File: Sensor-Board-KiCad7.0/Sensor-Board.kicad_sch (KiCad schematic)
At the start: 73 parts, among them J1 B4B-XH-A, U1 OPA396DCKT, U10 BME680, U13 TCA9548AMRGER, U14 OPA396DCKT, U19 MMBFJ177LT1, U2 OPA396DCKT, U20 MMBFJ177LT1, U21 OPA396DCKT, U22 OPA396DCKT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

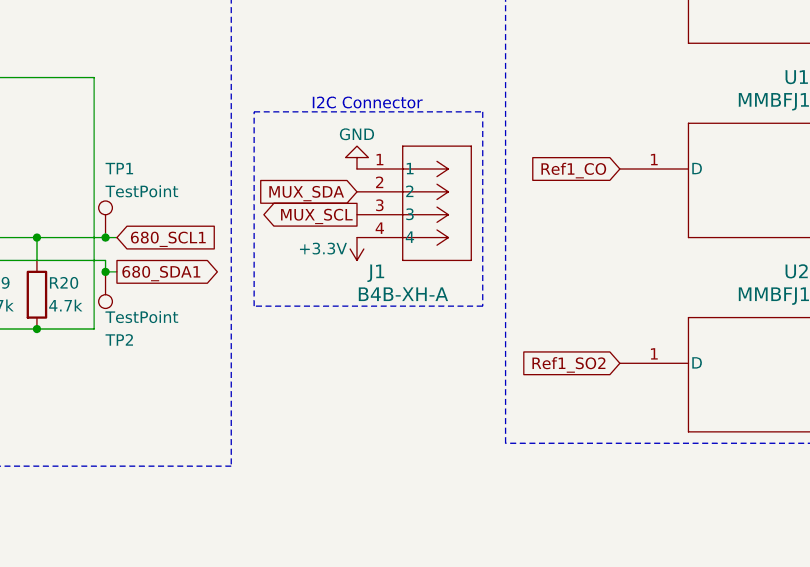
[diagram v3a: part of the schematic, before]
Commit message: Traces all connected v1.0
Restarted the process of routing traces (didn't account for width of 3.3V traces in first attempt). Everything is now connected for first time.
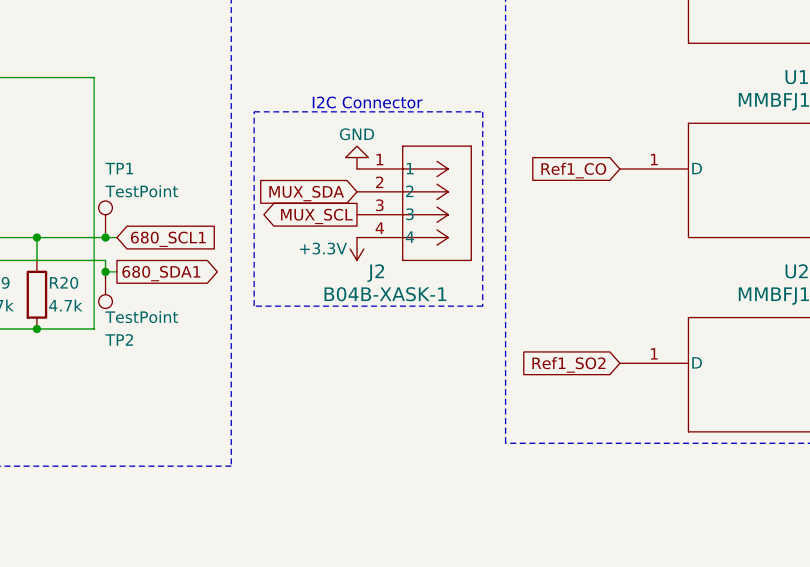
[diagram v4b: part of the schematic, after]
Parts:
- removed J1: B4B-XH-A, I2C Connector:CONN_B4B-XH-A_JST, symbol I2C Connector:B4B-XH-A
- added J2: B04B-XASK-1, B04B_XASK1:CONN_B04B-XASK-1_JST, symbol B04B_XASK_1:B04B-XASK-1
- U23: Digikey (none) -> ED90102-ND
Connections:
- net +3.3V: now also J2.4
- net GND: now also J2.1
- net MUX_SCL: now also J2.3
- net MUX_SDA: now also J2.2
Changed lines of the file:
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@@
       (effects (font (size 1.27 1.27)) hide)
     )
-    (property "Datasheet" "" (at 198.12 160.02 0)
+    (property "Datasheet" "ED90102-ND" (at 198.12 160.02 0)
       (effects (font (size 1.27 1.27)) hide)
     )
@@
       (effects (font (size 1.27 1.27)) hide)
     )
-    (property "Datasheet" "" (at 198.12 137.16 0)
+    (property "Datasheet" "ED90102-ND" (at 198.12 137.16 0)
       (effects (font (size 1.27 1.27)) hide)
     )
@@
       (effects (font (size 1.27 1.27)) hide)
     )
+    (property "Digikey" "ED90102-ND" (at 198.12 114.3 0)
+      (effects (font (size 1.27 1.27)) hide)
+    )
     (pin "3")
     (pin "1")
@@
     )
   )
+  (symbol (lib_id "B04B_XASK_1:B04B-XASK-1") (at 91.44 162.56 0) (unit 1)
+    (in_bom yes) (on_board yes) (dnp no)
+    (property "Reference" "J2" (at 92.71 173.99 0)
+      (effects (font (size 1.524 1.524)) (justify left))
+    )
+    (property "Value" "B04B-XASK-1" (at 87.63 176.53 0)
+      (effects (font (size 1.524 1.524)) (justify left))
+    )
+    (property "Footprint" "B04B_XASK1:CONN_B04B-XASK-1_JST" (at 88.9 156.21 0)
+      (effects (font (size 1.27 1.27) italic) hide)
+    )
+    (property "Datasheet" "B04B-XASK-1" (at 88.9 157.48 0)
+      (effects (font (size 1.27 1.27) italic) hide)
+    )
+    (property "LCSC" "C264994" (at 91.44 162.56 0)
+      (effects (font (size 1.27 1.27)) hide)
+    )
+    (pin "3")
+    (pin "1")
+    (pin "4")
+    (pin "2")
+    (instances
+      (project "Sensor-Board"
+        (path "/3a986dcd-349f-492d-950a-09832b2e5abd"
+          (reference "J2") (unit 1)
+        )
+      )
+    )
+  )
   (symbol (lib_id "Device:R") (at 109.22 77.47 270) (unit 1)
     (in_bom yes) (on_board yes) (dnp no)
@@
         )
       )
-    )
-  )
-  (symbol (lib_id "I2C Connector:B4B-XH-A") (at 91.44 162.56 0) (unit 1)
-    (in_bom yes) (on_board yes) (dnp no)
-    (property "Reference" "J1" (at 92.71 173.99 0)
-      (effects (font (size 1.524 1.524)) (justify left))
-    )
-    (property "Value" "B4B-XH-A" (at 91.44 176.53 0)
-      (effects (font (size 1.524 1.524)) (justify left))
-    )
-    (property "Footprint" "I2C Connector:CONN_B4B-XH-A_JST" (at 87.63 157.48 0)
-      (effects (font (size 1.27 1.27) italic) hide)
-    )
-    (property "Datasheet" "B4B-XH-A" (at 87.63 160.02 0)
-      (effects (font (size 1.27 1.27) italic) hide)
-    )
-    (pin "2")
-    (pin "4")
-    (pin "1")
-    (pin "3")
-    (instances
-      (project "Sensor-Board"
-        (path "/3a986dcd-349f-492d-950a-09832b2e5abd"
-          (reference "J1") (unit 1)
-        )
-      )

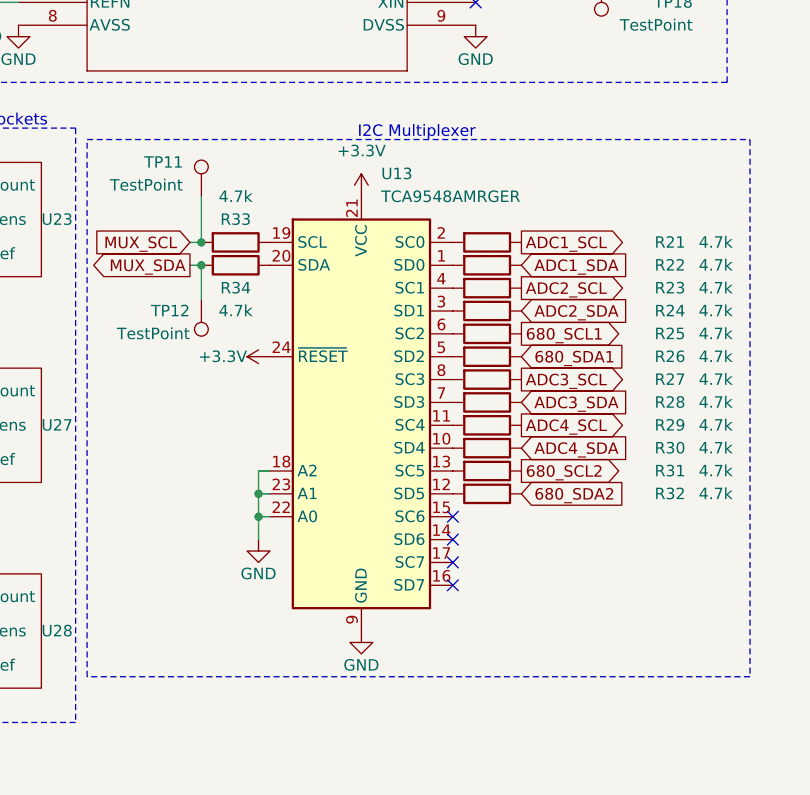
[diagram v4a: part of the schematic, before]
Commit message: Replaced TCA9548 footprint
Replaced TCA9548 footprint and added LCSC + Digikey numbers for all remaining symbols in schematic
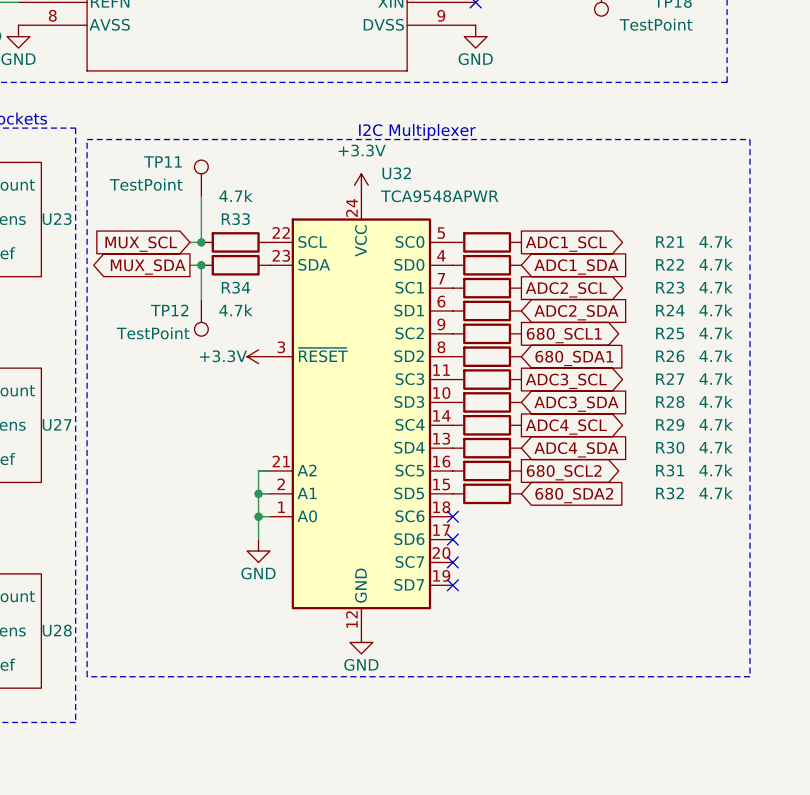
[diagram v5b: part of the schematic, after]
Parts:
- removed U13: TCA9548AMRGER, Package_DFN_QFN:Texas_RGE0024C_VQFN-24-1EP_4x4mm_P0.5mm_EP2.1x2.1mm, symbol Interface_Expansion:TCA9548AMRGER
- added U32: TCA9548APWR, Package_SO:TSSOP-24_4.4x7.8mm_P0.65mm, symbol Interface_Expansion:TCA9548APWR
- U1, U14, U21, U22: Digikey (none) -> 296-OPA396DCKRCT-ND
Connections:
- net +3.3V: now also U32.24 (VCC), U32.3 (~{RESET})
- net GND: now also U32.1 (A0), U32.12 (GND), U32.2 (A1), U32.21 (A2)
- net at R22.2: now also U32.4 (SD0)
- net at R30.2: now also U32.13 (SD4)
- net at R29.2: now also U32.14 (SC4)
- net at R32.2: now also U32.15 (SD5)
- net at R31.2: now also U32.16 (SC5)
- net at R33.1: now also U32.22 (SCL)
- net at R21.2: now also U32.5 (SC0)
- net at R34.1: now also U32.23 (SDA)
- net at R24.2: now also U32.6 (SD1)
- net at R23.2: now also U32.7 (SC1)
- net at R26.2: now also U32.8 (SD2)
- net at R25.2: now also U32.9 (SC2)
- net at R28.2: now also U32.10 (SD3)
- net at R27.2: now also U32.11 (SC3)
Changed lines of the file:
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@@
       (effects (font (size 1.27 1.27) italic) hide)
+    )
+    (property "Digikey" "296-OPA396DCKRCT-ND" (at 40.64 88.9 0)
+      (effects (font (size 1.27 1.27)) hide)
     )
     (pin "1")
@@
     )
   )
-  (symbol (lib_id "Interface_Expansion:TCA9548AMRGER") (at 240.03 128.27 0) (unit 1)
-    (in_bom yes) (on_board yes) (dnp no) (fields_autoplaced)
-    (property "Reference" "U13" (at 242.2241 102.87 0)
-      (effects (font (size 1.27 1.27)) (justify left))
-    )
-    (property "Value" "TCA9548AMRGER" (at 242.2241 105.41 0)
-      (effects (font (size 1.27 1.27)) (justify left))
-    )
-    (property "Footprint" "Package_DFN_QFN:Texas_RGE0024C_VQFN-24-1EP_4x4mm_P0.5mm_EP2.1x2.1mm" (at 240.03 153.67 0)
-      (effects (font (size 1.27 1.27)) hide)
-    )
-    (property "Datasheet" "http://www.ti.com/lit/ds/symlink/tca9548a.pdf" (at 241.3 121.92 0)
-      (effects (font (size 1.27 1.27)) hide)
-    )
-    (pin "10")
-    (pin "4")
-    (pin "14")
-    (pin "1")
-    (pin "2")
-    (pin "9")
-    (pin "5")
-    (pin "18")
-    (pin "12")
-    (pin "23")
-    (pin "8")
-    (pin "21")
-    (pin "25")
-    (pin "13")
-    (pin "11")
-    (pin "15")
-    (pin "16")
-    (pin "19")
-    (pin "20")
-    (pin "3")
-    (pin "17")
-    (pin "24")
-    (pin "6")
-    (pin "7")
-    (pin "22")
-    (instances
-      (project "Sensor-Board"
-        (path "/3a986dcd-349f-492d-950a-09832b2e5abd"
-          (reference "U13") (unit 1)
-        )
-      )
-    )
-  )
   (symbol (lib_id "Device:R") (at 254 135.89 270) (unit 1)
     (in_bom yes) (on_board yes) (dnp no)
@@
     (property "Datasheet" "OPA396DCKT" (at 40.64 130.81 0)
       (effects (font (size 1.27 1.27) italic) hide)
+    )
+    (property "Digikey" "296-OPA396DCKRCT-ND" (at 40.64 130.81 0)
+      (effects (font (size 1.27 1.27)) hide)
     )
     (pin "1")
@@
     (property "Datasheet" "OPA396DCKT" (at 113.03 77.47 0)
       (effects (font (size 1.27 1.27) italic) hide)
+    )
+    (property "Digikey" "" (at 113.03 77.47 0)
+      (effects (font (size 1.27 1.27)) hide)
     )
     (pin "1")
@@
       (effects (font (size 1.27 1.27) italic) hide)
     )
+    (property "Digikey" "296-OPA396DCKRCT-ND" (at 111.76 41.91 0)
+      (effects (font (size 1.27 1.27)) hide)
+    )
     (pin "1")
     (pin "3")
@@
       (effects (font (size 1.27 1.27) italic) hide)
     )
+    (property "Digikey" "296-OPA396DCKRCT-ND" (at 40.64 46.99 0)
+      (effects (font (size 1.27 1.27)) hide)
+    )
     (pin "1")
     (pin "3")
@@
       (effects (font (size 1.27 1.27) italic) hide)
     )
+    (property "Digikey" "" (at 113.03 113.03 0)
+      (effects (font (size 1.27 1.27)) hide)
+    )
     (pin "1")
     (pin "3")
@@
         )
       )
+    )
+  )
+  (symbol (lib_id "Interface_Expansion:TCA9548APWR") (at 240.03 128.27 0) (unit 1)
+    (in_bom yes) (on_board yes) (dnp no) (fields_autoplaced)
+    (property "Reference" "U32" (at 242.2241 102.87 0)
+      (effects (font (size 1.27 1.27)) (justify left))
+    )
+    (property "Value" "TCA9548APWR" (at 242.2241 105.41 0)
+      (effects (font (size 1.27 1.27)) (justify left))
+    )
+    (property "Footprint" "Package_SO:TSSOP-24_4.4x7.8mm_P0.65mm" (at 240.03 153.67 0)
+      (effects (font (size 1.27 1.27)) hide)
+    )
+    (property "Datasheet" "http://www.ti.com/lit/ds/symlink/tca9548a.pdf" (at 241.3 121.92 0)
+      (effects (font (size 1.27 1.27)) hide)
+    )
+    (property "LCSC" "C130026" (at 240.03 128.27 0)
+      (effects (font (size 1.27 1.27)) hide)
+    )
+    (pin "20")
+    (pin "23")
+    (pin "19")
+    (pin "4")
+    (pin "7")
+    (pin "12")
+    (pin "21")
+    (pin "8")
+    (pin "14")
+    (pin "6")
+    (pin "17")
+    (pin "11")
+    (pin "15")
+    (pin "18")
+    (pin "22")
+    (pin "1")
+    (pin "10")
+    (pin "2")
+    (pin "5")
+    (pin "13")
+    (pin "16")
+    (pin "24")
+    (pin "3")
+    (pin "9")
+    (instances
+      (project "Sensor-Board"
+        (path "/3a986dcd-349f-492d-950a-09832b2e5abd"
+          (reference "U32") (unit 1)
+        )
+      )

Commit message: Updated gas collection cell drawing
Updated GCC drawing to bring it to actual size
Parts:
- J2: Digikey (none) -> 455-2150-ND
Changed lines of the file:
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@@
+      (effects (font (size 1.27 1.27)) hide)
+    )
+    (property "Digikey" "455-2150-ND" (at 91.44 162.56 0)
       (effects (font (size 1.27 1.27)) hide)
     )

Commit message: Updated page settings
Added details such as contributors, Rev. number, board name, etc...
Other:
- company: (none) -> Queen's Rocket Engineering Team
- title: (none) -> Payload Sensor Board
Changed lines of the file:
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@@
 (kicad_sch (version 20230121) (generator eeschema)
   (paper "A4")
+  (title_block
+    (title "Payload Sensor Board")
+    (date "2024-03-23")
+    (rev "1.0")
+    (company "Queen's Rocket Engineering Team")
+    (comment 1 "Contributors: Kennan Bays, Joachim Blohm, Rowan Burke, Mohamad Gapre, Dominic Kilpatrick, Ben Taylor")
+  )
   (junction (at 153.67 67.31) (diameter 0) (color 0 0 0 0)
   )

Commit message: Updated part numbers
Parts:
- C4: LCSC (none) -> C140966
- J2: Digikey 455-2150-ND -> (none)
- U19, U20, U26: LCSC (none) -> C106763
- U2, U3: Digikey (none) -> 296-OPA396DCKRCT-ND
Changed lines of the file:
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@@
       (effects (font (size 1.27 1.27) italic) hide)
+    )
+    (property "LCSC" "C106763" (at 120.65 140.97 0)
+      (effects (font (size 1.27 1.27)) hide)
     )
     (pin "2")
@@
       (effects (font (size 1.27 1.27)) hide)
     )
+    (property "LCSC" "C140966" (at 189.23 39.37 0)
+      (effects (font (size 1.27 1.27)) hide)
+    )
     (pin "1")
     (pin "2")
@@
       (effects (font (size 1.27 1.27) italic) hide)
     )
+    (property "LCSC" "C106763" (at 120.65 162.56 0)
+      (effects (font (size 1.27 1.27)) hide)
+    )
     (pin "1")
     (pin "3")
@@
       (effects (font (size 1.27 1.27) italic) hide)
     )
-    (property "Digikey" "" (at 113.03 77.47 0)
+    (property "Digikey" "296-OPA396DCKRCT-ND" (at 113.03 77.47 0)
       (effects (font (size 1.27 1.27)) hide)
     )
@@
       (effects (font (size 1.27 1.27) italic) hide)
     )
+    (property "LCSC" "C106763" (at 120.65 184.15 0)
+      (effects (font (size 1.27 1.27)) hide)
+    )
     (pin "1")
     (pin "3")
@@
       (effects (font (size 1.27 1.27)) hide)
     )
-    (property "Digikey" "455-2150-ND" (at 91.44 162.56 0)
-      (effects (font (size 1.27 1.27)) hide)
-    )
     (pin "3")
     (pin "1")
@@
       (effects (font (size 1.27 1.27) italic) hide)
     )
-    (property "Digikey" "" (at 113.03 113.03 0)
-      (effects (font (size 1.27 1.27)) hide)
-    )
+    (property "Digikey" "296-OPA396DCKRCT-ND" (at 113.03 113.03 0)
+      (effects (font (size 1.27 1.27)) hide)
+    )
